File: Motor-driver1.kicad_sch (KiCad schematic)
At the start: 32 parts, among them J8 PINHD_1x4_Male, J9 PINHD_1x4_Male, U2 DRV8825PWP, U3 DRV8825PWP

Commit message: deTommaso approved version
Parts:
- removed RV3: R_Potentiometer, poti:3386P1473LF, symbol Device:R_Potentiometer
- removed TP6 (x2): TestPoint, TestPoint:TestPoint_Pad_D1.5mm, symbol Connector:TestPoint
- added RV2: R_Potentiometer, poti:3386P1473LF, symbol Device:R_Potentiometer
- C18, C22: value Bulk Capacitance. 4.7uF? -> 10uF; footprint Capacitor_SMD:C_0805_2012Metric -> Capacitor_THT:C_Radial_D5.0mm_H5.0mm_P2.00mm
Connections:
- net GND: now also RV2.2
- net at R20.1, U2.12 (AVREF), U2.13 (BVREF): now also RV2.1
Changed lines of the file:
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@@
   (junction (at 255.905 34.29) (diameter 0) (color 0 0 0 0)
   )
-  (junction (at 207.01 53.34) (diameter 0) (color 0 0 0 0)
-  )
   (junction (at 86.36 125.73) (diameter 0) (color 0 0 0 0)
-  )
-  (junction (at 74.93 111.76) (diameter 0) (color 0 0 0 0)
   )
   (junction (at 123.19 163.83) (diameter 0) (color 0 0 0 0)
@@
     (stroke (width 0) (type default))
   )
-  (wire (pts (xy 207.01 53.34) (xy 218.44 53.34))
-    (stroke (width 0) (type default))
-  )
   (wire (pts (xy 254.635 44.45) (xy 255.905 44.45))
     (stroke (width 0) (type default))
@@
     (stroke (width 0) (type default))
   )
-  (wire (pts (xy 201.93 53.34) (xy 207.01 53.34))
+  (wire (pts (xy 201.93 53.34) (xy 218.44 53.34))
     (stroke (width 0) (type default))
   )
@@
     (stroke (width 0) (type default))
   )
-  (wire (pts (xy 69.85 111.76) (xy 74.93 111.76))
+  (wire (pts (xy 69.85 111.76) (xy 86.36 111.76))
     (stroke (width 0) (type default))
   )
@@
   )
   (wire (pts (xy 262.89 59.69) (xy 262.255 59.69))
-    (stroke (width 0) (type default))
-  )
-  (wire (pts (xy 86.36 111.76) (xy 74.93 111.76))
     (stroke (width 0) (type default))
   )
@@
     )
   )
-  (symbol (lib_id "Connector:TestPoint") (at 74.93 111.76 0) (unit 1)
-    (in_bom yes) (on_board yes) (dnp no)
-    (property "Reference" "TP6" (at 75.565 104.14 90)
-      (effects (font (size 1.27 1.27)))
-    )
-    (property "Value" "TestPoint" (at 75.565 95.885 90)
-      (effects (font (size 1.27 1.27)))
-    )
-    (property "Footprint" "TestPoint:TestPoint_Pad_D1.5mm" (at 80.01 111.76 0)
-      (effects (font (size 1.27 1.27)) hide)
-    )
-    (property "Datasheet" "~" (at 80.01 111.76 0)
-      (effects (font (size 1.27 1.27)) hide)
-    )
-    (pin "1")
-    (instances
-      (project "Doodle Drive"
-        (path "/3ec634aa-8c09-482d-9325-2288a4dbd68b/4a4951fa-be57-4d48-97a5-6be750b353b5"
-          (reference "TP6") (unit 1)
-        )
-        (path "/3ec634aa-8c09-482d-9325-2288a4dbd68b/ce40ab82-c304-4dd2-80f5-b6df1964b151"
-          (reference "TP42") (unit 1)
-        )
-        (path "/3ec634aa-8c09-482d-9325-2288a4dbd68b/bef0954e-6024-4756-b9a6-5ea2a0825f13"
-          (reference "TP54") (unit 1)
-        )
-      )
-    )
-  )
   (symbol (lib_id "power:GND") (at 133.985 107.95 0) (unit 1)
     (in_bom yes) (on_board yes) (dnp no)
@@
         (path "/3ec634aa-8c09-482d-9325-2288a4dbd68b/bef0954e-6024-4756-b9a6-5ea2a0825f13"
           (reference "RV4") (unit 1)
-        )
-      )
-    )
-  )
-  (symbol (lib_id "Device:R_Potentiometer") (at 201.93 57.785 0) (unit 1)
-    (in_bom yes) (on_board yes) (dnp no)
-    (property "Reference" "RV3" (at 199.39 56.515 90)
-      (effects (font (size 1.27 1.27)) (justify right))
-    )
-    (property "Value" "R_Potentiometer" (at 203.835 62.865 0)
-      (effects (font (size 1.27 1.27)) (justify right))
-    )
-    (property "Footprint" "poti:3386P1473LF" (at 201.93 57.785 0)
-      (effects (font (size 1.27 1.27)) hide)
-    )
-    (property "Datasheet" "~" (at 201.93 57.785 0)
-      (effects (font (size 1.27 1.27)) hide)
-    )
-    (pin "1")
-    (pin "2")
-    (pin "3")
-    (instances
-      (project "Doodle Drive"
-        (path "/3ec634aa-8c09-482d-9325-2288a4dbd68b/4a4951fa-be57-4d48-97a5-6be750b353b5"
-          (reference "RV3") (unit 1)
-        )
-        (path "/3ec634aa-8c09-482d-9325-2288a4dbd68b/ce40ab82-c304-4dd2-80f5-b6df1964b151"
-          (reference "RV1") (unit 1)
-        )
-        (path "/3ec634aa-8c09-482d-9325-2288a4dbd68b/bef0954e-6024-4756-b9a6-5ea2a0825f13"
-          (reference "RV7") (unit 1)
         )
       )
@@
       (effects (font (size 1.27 1.27)))
     )
-    (property "Value" "Bulk Capacitance. 4.7uF?" (at 135.255 88.9 90)
-      (effects (font (size 1.27 1.27)))
-    )
-    (property "Footprint" "Capacitor_SMD:C_0805_2012Metric" (at 125.095 93.6752 0)
+    (property "Value" "10uF" (at 129.54 88.9 90)
+      (effects (font (size 1.27 1.27)))
+    )
+    (property "Footprint" "Capacitor_THT:C_Radial_D5.0mm_H5.0mm_P2.00mm" (at 125.095 93.6752 0)
       (effects (font (size 1.27 1.27)) hide)
     )
@@
         (path "/3ec634aa-8c09-482d-9325-2288a4dbd68b/bef0954e-6024-4756-b9a6-5ea2a0825f13"
           (reference "C37") (unit 1)
-        )
-      )
-    )
-  )
-  (symbol (lib_id "Connector:TestPoint") (at 207.01 53.34 0) (unit 1)
-    (in_bom yes) (on_board yes) (dnp no)
-    (property "Reference" "TP6" (at 207.645 45.72 90)
-      (effects (font (size 1.27 1.27)))
-    )
-    (property "Value" "TestPoint" (at 207.645 37.465 90)
-      (effects (font (size 1.27 1.27)))
-    )
-    (property "Footprint" "TestPoint:TestPoint_Pad_D1.5mm" (at 212.09 53.34 0)
-      (effects (font (size 1.27 1.27)) hide)
-    )
-    (property "Datasheet" "~" (at 212.09 53.34 0)
-      (effects (font (size 1.27 1.27)) hide)
-    )
-    (pin "1")
-    (instances
-      (project "Doodle Drive"
-        (path "/3ec634aa-8c09-482d-9325-2288a4dbd68b/4a4951fa-be57-4d48-97a5-6be750b353b5"
-          (reference "TP6") (unit 1)
-        )
-        (path "/3ec634aa-8c09-482d-9325-2288a4dbd68b/ce40ab82-c304-4dd2-80f5-b6df1964b151"
-          (reference "TP1") (unit 1)
-        )
-        (path "/3ec634aa-8c09-482d-9325-2288a4dbd68b/bef0954e-6024-4756-b9a6-5ea2a0825f13"
-          (reference "TP62") (unit 1)
         )
       )
@@
         (path "/3ec634aa-8c09-482d-9325-2288a4dbd68b/bef0954e-6024-4756-b9a6-5ea2a0825f13"
           (reference "R32") (unit 1)
-        )
-      )
-    )
-  )
-  (symbol (lib_id "Device:C") (at 260.985 34.29 270) (unit 1)
-    (in_bom yes) (on_board yes) (dnp no)
-    (property "Reference" "C18" (at 260.985 27.305 90)
-      (effects (font (size 1.27 1.27)))
-    )
-    (property "Value" "Bulk Capacitance. 4.7uF?" (at 267.335 30.48 90)
-      (effects (font (size 1.27 1.27)))
-    )
-    (property "Footprint" "Capacitor_SMD:C_0805_2012Metric" (at 257.175 35.2552 0)
-      (effects (font (size 1.27 1.27)) hide)
-    )
-    (property "Datasheet" "~" (at 260.985 34.29 0)
-      (effects (font (size 1.27 1.27)) hide)
-    )
-    (pin "1")
-    (pin "2")
-    (instances
-      (project "Doodle Drive"
-        (path "/3ec634aa-8c09-482d-9325-2288a4dbd68b/ce40ab82-c304-4dd2-80f5-b6df1964b151"
-          (reference "C18") (unit 1)
-        )
-        (path "/3ec634aa-8c09-482d-9325-2288a4dbd68b/bef0954e-6024-4756-b9a6-5ea2a0825f13"
-          (reference "C42") (unit 1)
         )
       )
@@
     )
   )
+  (symbol (lib_id "Device:R_Potentiometer") (at 201.93 57.785 0) (unit 1)
+    (in_bom yes) (on_board yes) (dnp no)
+    (property "Reference" "RV2" (at 194.31 56.515 90)
+      (effects (font (size 1.27 1.27)) (justify right))
+    )
+    (property "Value" "R_Potentiometer" (at 203.835 62.865 0)
+      (effects (font (size 1.27 1.27)) (justify right))
+    )
+    (property "Footprint" "poti:3386P1473LF" (at 201.93 57.785 0)
+      (effects (font (size 1.27 1.27)) hide)
+    )
+    (property "Datasheet" "~" (at 201.93 57.785 0)
+      (effects (font (size 1.27 1.27)) hide)
+    )
+    (pin "1")
+    (pin "2")
+    (pin "3")
+    (instances
+      (project "Doodle Drive"
+        (path "/3ec634aa-8c09-482d-9325-2288a4dbd68b/4a4951fa-be57-4d48-97a5-6be750b353b5"
+          (reference "RV2") (unit 1)
+        )
+        (path "/3ec634aa-8c09-482d-9325-2288a4dbd68b/ce40ab82-c304-4dd2-80f5-b6df1964b151"
+          (reference "RV1") (unit 1)
+        )
+      )
+    )
+  )
   (symbol (lib_id "Device:C") (at 128.905 97.79 90) (unit 1)
     (in_bom yes) (on_board yes) (dnp no)
@@
         )
       )
+    )
+  )
+  (symbol (lib_id "Device:C") (at 260.985 34.29 270) (unit 1)
+    (in_bom yes) (on_board yes) (dnp no)
+    (property "Reference" "C18" (at 260.985 27.305 90)
+      (effects (font (size 1.27 1.27)))
+    )
+    (property "Value" "10uF" (at 261.62 30.48 90)
+      (effects (font (size 1.27 1.27)))
+    )
+    (property "Footprint" "Capacitor_THT:C_Radial_D5.0mm_H5.0mm_P2.00mm" (at 257.175 35.2552 0)
+      (effects (font (size 1.27 1.27)) hide)
+    )
+    (property "Datasheet" "~" (at 260.985 34.29 0)
+      (effects (font (size 1.27 1.27)) hide)
+    )
+    (pin "1")
+    (pin "2")
+    (instances
+      (project "Doodle Drive"
+        (path "/3ec634aa-8c09-482d-9325-2288a4dbd68b/ce40ab82-c304-4dd2-80f5-b6df1964b151"
+          (reference "C18") (unit 1)
+        )
+        (path "/3ec634aa-8c09-482d-9325-2288a4dbd68b/bef0954e-6024-4756-b9a6-5ea2a0825f13"
+          (reference "C37") (unit 1)
+        )
+      )

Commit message: bestellte version
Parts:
- C11, C16: value 100nF 16V ceramic -> 100nF
- C15, C5: value 10nF 50V -> 10nF
- C20, C21, C23, C24: value 100nF 50V -> 100nF
- R12, R13, R15, R16: footprint Resistor_SMD:R_0805_2012Metric -> Resistor_SMD:R_1206_3216Metric
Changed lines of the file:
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@@
       (effects (font (size 1.27 1.27)))
     )
-    (property "Footprint" "Resistor_SMD:R_0805_2012Metric" (at 214.884 97.028 0)
+    (property "Footprint" "Resistor_SMD:R_1206_3216Metric" (at 214.884 97.028 0)
       (effects (font (size 1.27 1.27)) hide)
     )
@@
       (effects (font (size 1.27 1.27)) (justify left))
     )
-    (property "Value" "10nF 50V" (at 199.39 80.645 90)
+    (property "Value" "10nF" (at 199.39 80.645 90)
       (effects (font (size 1.27 1.27)) (justify left))
     )
@@
       (effects (font (size 1.27 1.27)))
     )
-    (property "Value" "100nF 50V" (at 139.7 102.87 90)
+    (property "Value" "100nF" (at 139.7 102.87 90)
       (effects (font (size 1.27 1.27)))
     )
@@
       (effects (font (size 1.27 1.27)) (justify left))
     )
-    (property "Value" "10nF 50V" (at 67.31 139.065 90)
+    (property "Value" "10nF" (at 67.31 139.065 90)
       (effects (font (size 1.27 1.27)) (justify left))
     )
@@
       (effects (font (size 1.27 1.27)) (justify left))
     )
-    (property "Value" "100nF 16V ceramic" (at 90.17 158.75 90)
+    (property "Value" "100nF" (at 90.17 158.75 90)
       (effects (font (size 1.27 1.27)) (justify left))
     )
@@
       (effects (font (size 1.27 1.27)))
     )
-    (property "Value" "100nF 50V" (at 140.335 97.79 90)
+    (property "Value" "100nF" (at 140.335 97.79 90)
       (effects (font (size 1.27 1.27)))
     )
@@
       (effects (font (size 1.27 1.27)))
     )
-    (property "Value" "100nF 50V" (at 272.415 39.37 90)
+    (property "Value" "100nF" (at 272.415 39.37 90)
       (effects (font (size 1.27 1.27)))
     )
@@
       (effects (font (size 1.27 1.27)) (justify left))
     )
-    (property "Value" "100nF 16V ceramic" (at 222.25 100.33 90)
+    (property "Value" "100nF" (at 222.25 100.33 90)
       (effects (font (size 1.27 1.27)) (justify left))
     )
@@
       (effects (font (size 1.27 1.27)))
     )
-    (property "Footprint" "Resistor_SMD:R_0805_2012Metric" (at 82.804 155.448 0)
+    (property "Footprint" "Resistor_SMD:R_1206_3216Metric" (at 82.804 155.448 0)
       (effects (font (size 1.27 1.27)) hide)
     )
@@
       (effects (font (size 1.27 1.27)))
     )
-    (property "Value" "100nF 50V" (at 271.78 44.45 90)
+    (property "Value" "100nF" (at 271.78 44.45 90)
       (effects (font (size 1.27 1.27)))
     )
@@
       (effects (font (size 1.27 1.27)) (justify right))
     )
-    (property "Footprint" "Resistor_SMD:R_0805_2012Metric" (at 213.106 83.312 0)
+    (property "Footprint" "Resistor_SMD:R_1206_3216Metric" (at 213.106 83.312 0)
       (effects (font (size 1.27 1.27)) hide)
     )
@@
       (effects (font (size 1.27 1.27)) (justify right))
     )
-    (property "Footprint" "Resistor_SMD:R_0805_2012Metric" (at 81.026 141.732 0)
-      (effects (font (size 1.27 1.27)) hide)
-    )
+    (property "Footprint" "Resistor_SMD:R_1206_3216Metric" (at 81.026 141.732 0)
+      (effects (font (size 1.27 1.27)) hide)
+    )

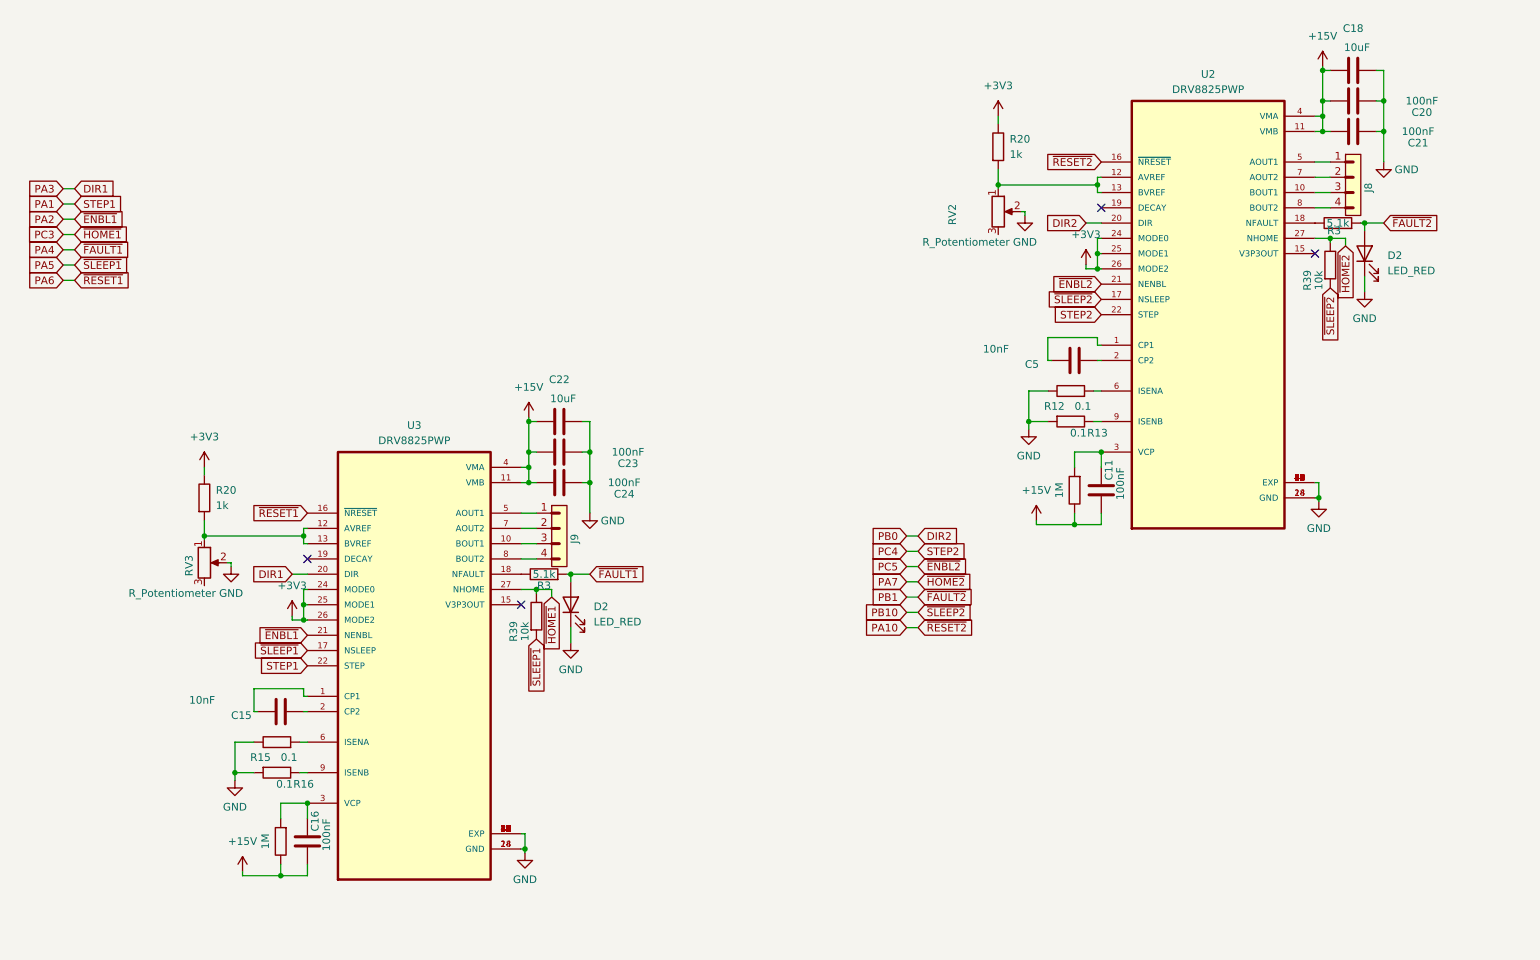
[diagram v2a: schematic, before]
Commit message: placed jlcpcb basic buttons and rerouted unchristliche wires
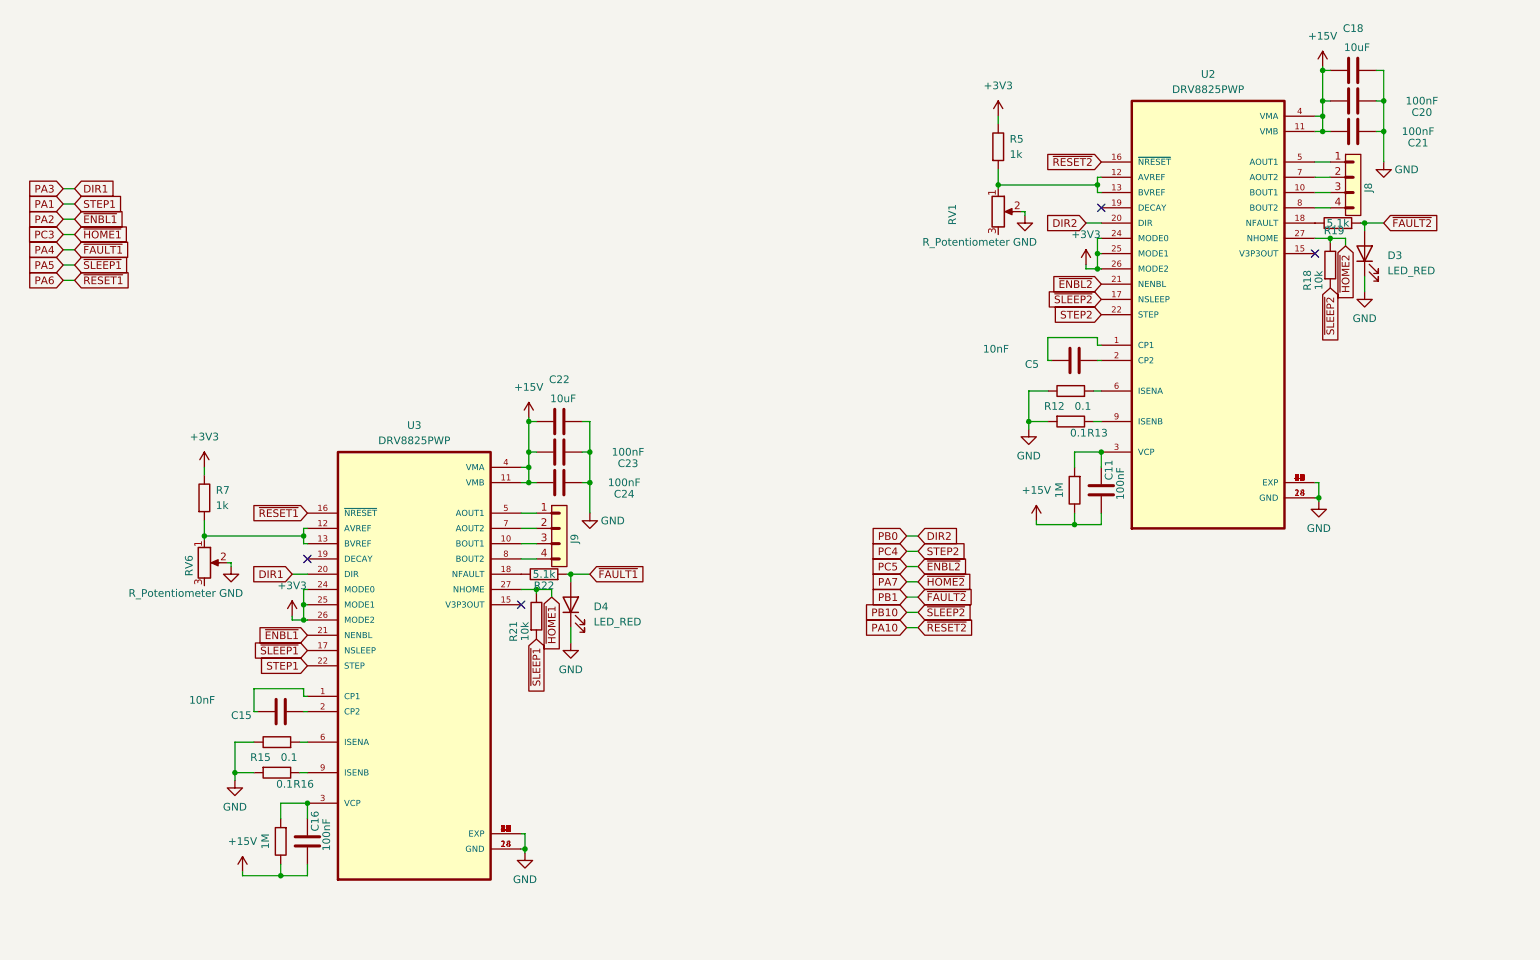
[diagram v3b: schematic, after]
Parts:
- renumbered D2 to D3, D2 to D4, R39 to R18, R3 to R19, R39 to R21, R3 to R22, R20 to R5, R20 to R7, RV2 to RV1, RV3 to RV6
